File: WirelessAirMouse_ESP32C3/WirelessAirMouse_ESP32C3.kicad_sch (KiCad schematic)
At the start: 9 parts, among them U1 ESP32-S3-SuperMini, U2 MPU-6050

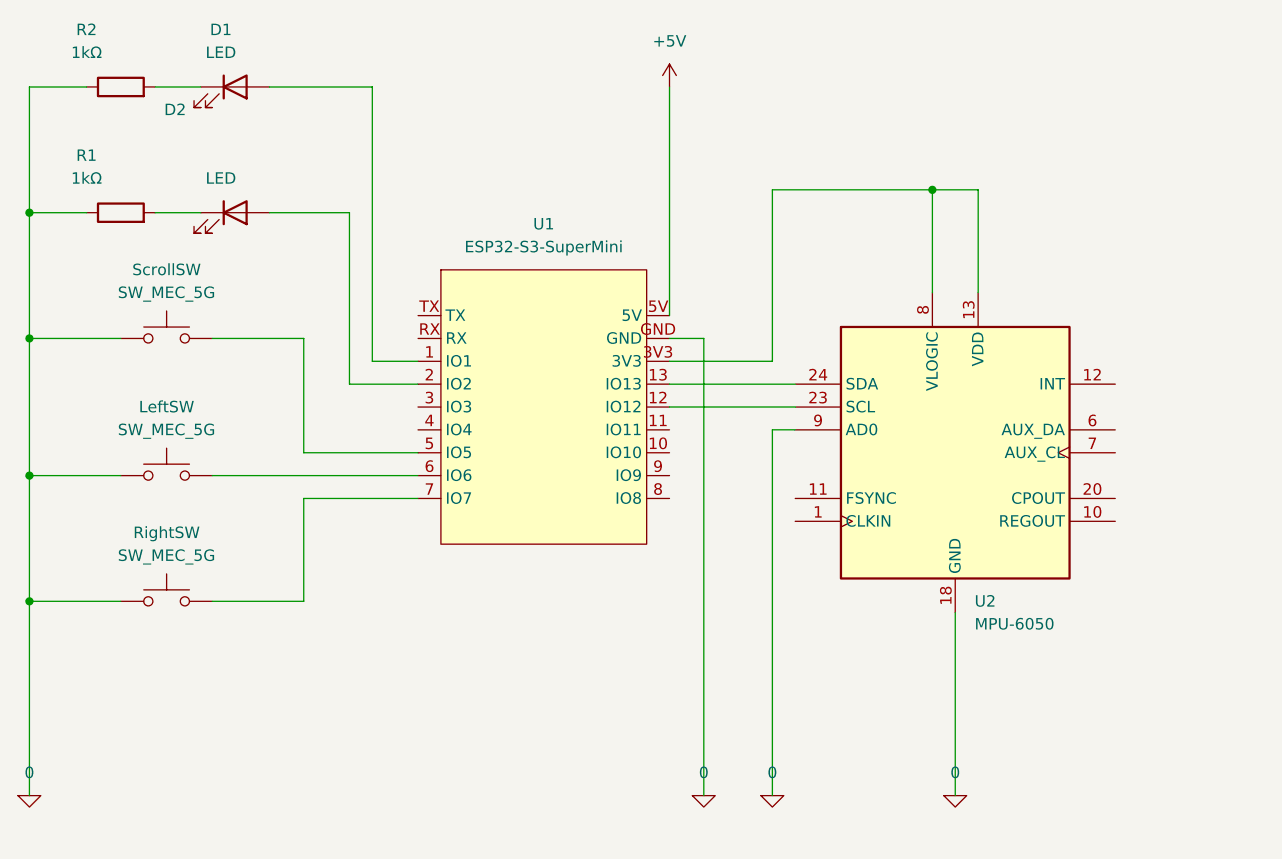
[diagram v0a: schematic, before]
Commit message: feat: add ESP32-C3 schematics, breadboard prototype, and separate C3/S3 KiCad projects
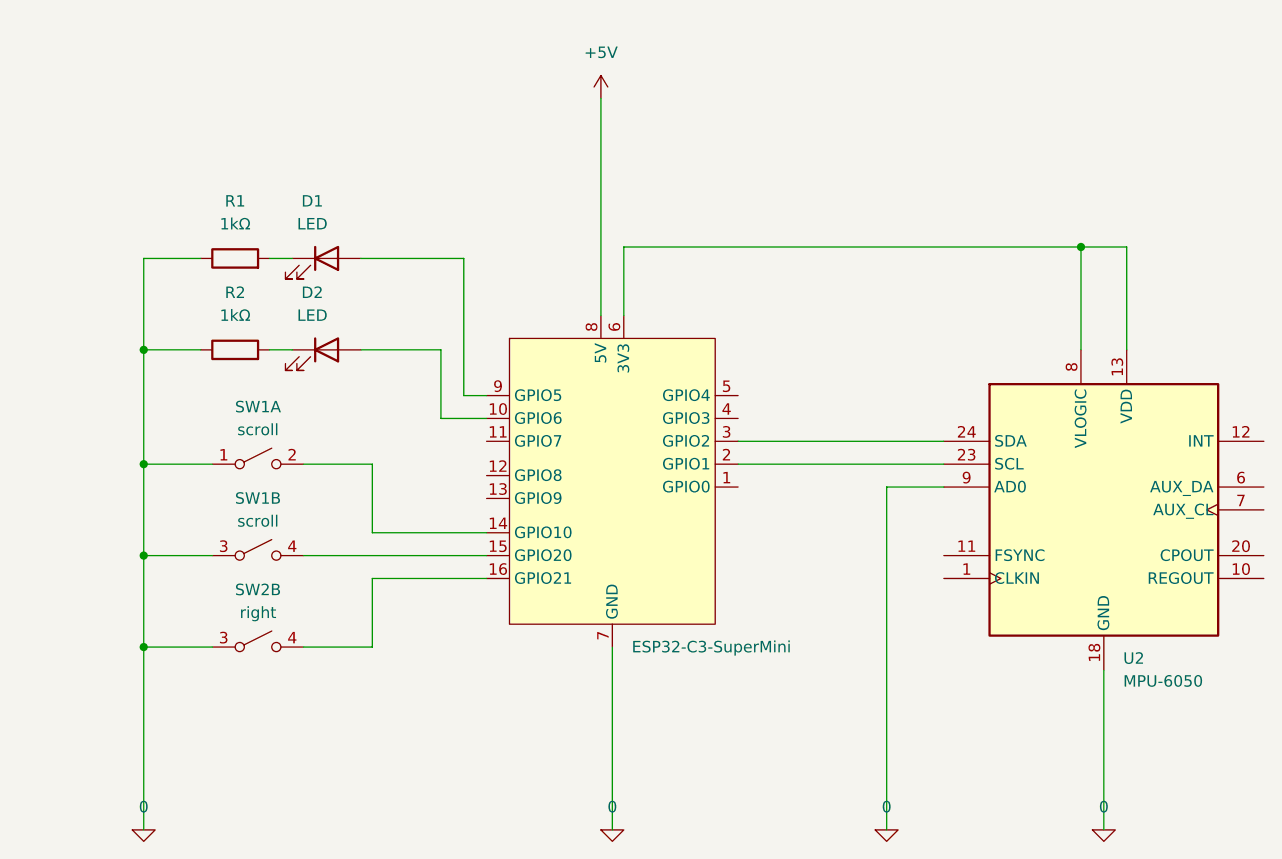
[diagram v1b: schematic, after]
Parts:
- removed LeftSW, RightSW, ScrollSW: SW_MEC_5G, symbol Switch:SW_MEC_5G
- removed U1: ESP32-S3-SuperMini, ESP32-S3-SuperMini:ESP32-S3-SuperMini, symbol ESP32-S3-SuperMini:ESP32-S3-SuperMini
- added SW1: scroll, symbol Switch:SW_DPST_x2
- added SW2: right, symbol Switch:SW_DPST_x2
- added U1: ESP32-C3-SuperMini, ESP32-C3-SuperMini:ESP32-C3-SuperMini, symbol ESP32-C3-SuperMini:ESP32-C3-SuperMini
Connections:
- net +5V: now also U1.8 (5V)
- net 0: now also SW1.1 (A), SW1.3 (A), SW2.3 (A), U1.7 (GND)
- net at U2.13 (VDD), U2.8 (VLOGIC): now also U1.6 (3V3)
- net at U2.23 (SCL): now also U1.2 (GPIO1)
- net at U2.24 (SDA): now also U1.3 (GPIO2)
- net at D2.1 (K): now also R2.2; no longer R1.2
- net at D1.1 (K): now also R1.2; no longer R2.2
- net at D1.2 (A): now also U1.9 (GPIO5)
- net at D2.2 (A): now also U1.10 (GPIO6)
- new net: SW2.4 (B), U1.16 (GPIO21)
- new net: SW1.4 (B), U1.15 (GPIO20)
- new net: SW1.2 (B), U1.14 (GPIO10)
